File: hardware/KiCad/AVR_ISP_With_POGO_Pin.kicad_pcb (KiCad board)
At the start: 2 copper layers, 15.6 x 28.5 mm, 6 parts, among them P1 75869-131LF, P2 P50-B1

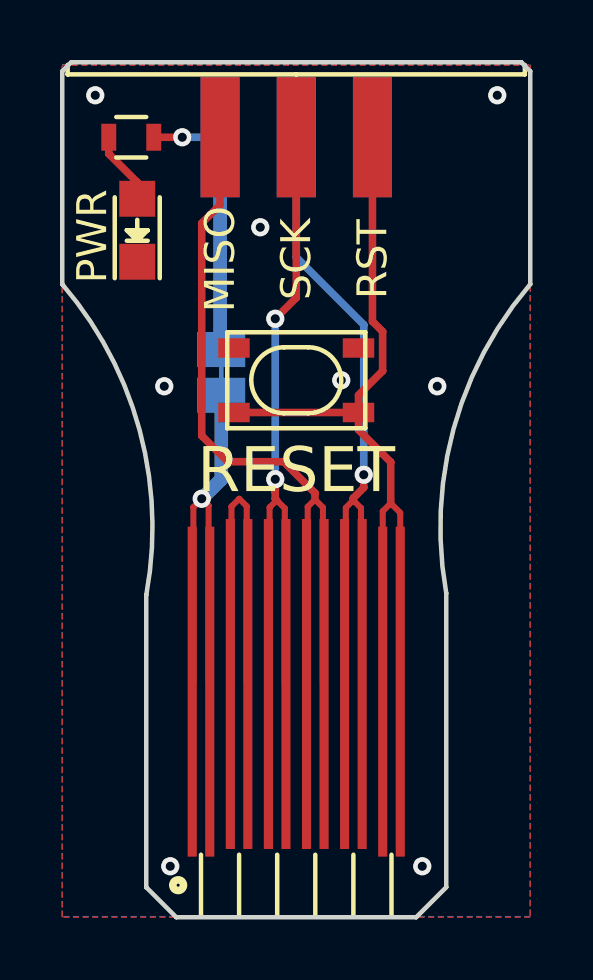
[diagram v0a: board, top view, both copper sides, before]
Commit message: Pour keepouts, spaces
More Space to Pads of Switch, Pour keepouts added.
All for making hand soldering more easy
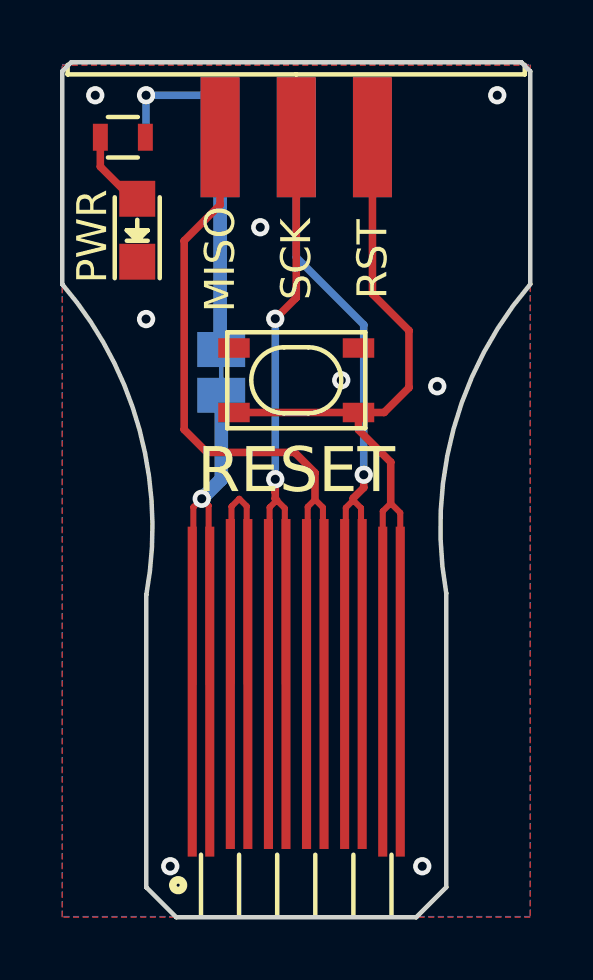
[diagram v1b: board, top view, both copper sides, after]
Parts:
- moved R1 0.28 mm to (137.2, 97.8)
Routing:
- net /VCC: track 27.1 -> 31.8 mm
- net /RESET: track 30.3 -> 31.5 mm
- net /MISO: track 27.5 -> 28.6 mm

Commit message: Added JLC Pattern for Order#
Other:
- board text added: "JLCJLCJLCJLC"
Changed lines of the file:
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@@
   (general
     (thickness 1.6)
-    (drawings 25)
+    (drawings 26)
     (tracks 81)
     (zones 0)
@@
   (page A4)
   (layers
-    (0 F.Cu signal)
-    (31 B.Cu signal hide)
+    (0 F.Cu signal hide)
+    (31 B.Cu signal)
     (32 B.Adhes user hide)
     (33 F.Adhes user hide)
-    (34 B.Paste user hide)
-    (35 F.Paste user)
-    (36 B.SilkS user hide)
-    (37 F.SilkS user)
-    (38 B.Mask user hide)
-    (39 F.Mask user)
+    (34 B.Paste user)
+    (35 F.Paste user hide)
+    (36 B.SilkS user)
+    (37 F.SilkS user hide)
+    (38 B.Mask user)
+    (39 F.Mask user hide)
     (40 Dwgs.User user hide)
     (41 Cmts.User user hide)
@@
     (44 Edge.Cuts user)
     (45 Margin user hide)
-    (46 B.CrtYd user hide)
-    (47 F.CrtYd user)
-    (48 B.Fab user hide)
-    (49 F.Fab user)
+    (46 B.CrtYd user)
+    (47 F.CrtYd user hide)
+    (48 B.Fab user)
+    (49 F.Fab user hide)
   )
   (setup
@@
     )
   )
+  (gr_text JLCJLCJLCJLC (at 146.503 109.449 -90) (layer B.Mask)
+    (effects (font (size 1.2 1.2) (thickness 0.18)) (justify mirror))
+  )
   (gr_text RST (at 146.2 119.7 90) (layer B.SilkS)
     (effects (font (size 1 1) (thickness 0.15)) (justify left mirror))
@@
     (polygon
       (pts
-        (xy 138.502 98.273) (xy 136.47 98.273) (xy 136.47 97.257) (xy 138.502 97.257)
+        (xy 138.502 98.4635) (xy 136.47 98.4635) (xy 136.47 97.13) (xy 138.502 97.13)
       )
     )
@@
     (polygon
       (pts
-        (xy 138.502 101.321) (xy 136.851 101.321) (xy 136.851 99.035) (xy 138.502 99.035)
-      )
-    )
+        (xy 138.502 101.321) (xy 136.851 101.321) (xy 136.851 97.13) (xy 138.502 97.13)
+      )
+    )
